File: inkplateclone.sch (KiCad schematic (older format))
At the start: 90 parts, among them J1 ED060SC7, J2 USB_C_Receptacle_USB2.0, J3 Conn_01x03_Male, Q1 Q_NMOS_GSD, Q2 Q_NMOS_GSD, Q3 Q_PMOS_GSD, U1 TPS65186, U2 ED097OC1, U3 MCP23017_SO, U4 ESP32-WROVER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

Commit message: removed polyfuses, fixes #2
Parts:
- removed F1, F2: Polyfuse, Fuse:Fuse_1206_3216Metric, symbol Device:Polyfuse
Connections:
- net +5V: now also J2.A4 (VBUS), J2.A9 (VBUS), J2.B4 (VBUS), J2.B9 (VBUS)
- net VBAT: now also C39.2, U9.5 (BAT)
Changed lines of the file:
@@
 Wire Wire Line
 	2000 9050 2200 9050
-Wire Wire Line
-	2200 9050 2200 8900
 $Comp
 L power:GND #PWR049
@@
 	1    0    0    -1
 $EndComp
-$Comp
-L Device:Polyfuse F1
-U 1 1 5F1AD48B
-P 15500 8600
-F 0 "F1" H 15588 8646 50  0000 L CNN
-F 1 "Polyfuse" H 15588 8555 50  0000 L CNN
-F 2 "Fuse:Fuse_1206_3216Metric" H 15550 8400 50  0001 L CNN
-F 3 "~" H 15500 8600 50  0001 C CNN
-	1    15500 8600
-	1    0    0    -1
-$EndComp
-Connection ~ 15500 8750
 Connection ~ 10100 8350
 Wire Wire Line
@@
 Text GLabel 15500 8400 1    50   Input ~ 0
 VBAT
-Wire Wire Line
-	15500 8400 15500 8450
 Text GLabel 14700 9050 2    50   Input ~ 0
 BAT_TMP
@@
 Wire Notes Line
 	500  7950 16050 7950
-$Comp
-L Device:Polyfuse F2
-U 1 1 5F977BD5
-P 2200 8750
-F 0 "F2" H 2288 8796 50  0000 L CNN
-F 1 "Polyfuse" H 2288 8705 50  0000 L CNN
-F 2 "Fuse:Fuse_1206_3216Metric" H 2250 8550 50  0001 L CNN
-F 3 "~" H 2200 8750 50  0001 C CNN
-	1    2200 8750
-	1    0    0    -1
-$EndComp
 Text Notes 11450 8250 0    100  ~ 0
 Protection and Charger
+Wire Wire Line
+	15500 8400 15500 8750
+Connection ~ 15500 8750
+Wire Wire Line
+	2200 8600 2200 9050
 $EndSCHEMATC

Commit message: replaced LDO, fixes #1
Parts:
- U6: value AMS1117-3.3 -> AP2114H-3.3TRG1
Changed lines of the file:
@@
 P 8550 10300
 F 0 "U6" H 8550 10542 50  0000 C CNN
-F 1 "AMS1117-3.3" H 8550 10451 50  0000 C CNN
+F 1 "AP2114H-3.3TRG1" H 8550 10451 50  0000 C CNN
 F 2 "Package_TO_SOT_SMD:SOT-223-3_TabPin2" H 8550 10500 50  0001 C CNN
 F 3 "http://www.advanced-monolithic.com/pdf/ds1117.pdf" H 8650 10050 50  0001 C CNN

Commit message: routed the usb c serial connection and went to town with alignment
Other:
- moved on the sheet: C29
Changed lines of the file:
@@
 U 1 1 5EADC962
 P 1500 1500
-F 0 "C1" V 1248 1500 50  0000 C CNN
-F 1 "4u7" V 1339 1500 50  0000 C CNN
+F 0 "C1" V 1350 1400 50  0000 C CNN
+F 1 "4u7" V 1350 1600 50  0000 C CNN
 F 2 "Capacitor_SMD:C_0805_2012Metric" H 1538 1350 50  0001 C CNN
 F 3 "~" H 1500 1500 50  0001 C CNN
@@
 U 1 1 5EADDF92
 P 1500 1850
-F 0 "C2" V 1248 1850 50  0000 C CNN
-F 1 "4u7" V 1339 1850 50  0000 C CNN
+F 0 "C2" V 1350 1750 50  0000 C CNN
+F 1 "4u7" V 1350 1950 50  0000 C CNN
 F 2 "Capacitor_SMD:C_0805_2012Metric" H 1538 1700 50  0001 C CNN
 F 3 "~" H 1500 1850 50  0001 C CNN
@@
 U 1 1 5EAE1BDC
 P 1500 2450
-F 0 "C4" V 1248 2450 50  0000 C CNN
-F 1 "10uF" V 1339 2450 50  0000 C CNN
+F 0 "C4" V 1350 2350 50  0000 C CNN
+F 1 "10uF" V 1350 2550 50  0000 C CNN
 F 2 "Capacitor_SMD:C_1206_3216Metric" H 1538 2300 50  0001 C CNN
 F 3 "~" H 1500 2450 50  0001 C CNN
@@
 U 1 1 5EAE31E3
 P 1500 2150
-F 0 "C3" V 1248 2150 50  0000 C CNN
-F 1 "4u7" V 1339 2150 50  0000 C CNN
+F 0 "C3" V 1350 2050 50  0000 C CNN
+F 1 "4u7" V 1350 2250 50  0000 C CNN
 F 2 "Capacitor_SMD:C_0805_2012Metric" H 1538 2000 50  0001 C CNN
 F 3 "~" H 1500 2150 50  0001 C CNN
@@
 U 1 1 5EAE4665
 P 1500 2850
-F 0 "C5" V 1248 2850 50  0000 C CNN
-F 1 "4u7" V 1339 2850 50  0000 C CNN
+F 0 "C5" V 1350 2750 50  0000 C CNN
+F 1 "4u7" V 1350 2950 50  0000 C CNN
 F 2 "Capacitor_SMD:C_0805_2012Metric" H 1538 2700 50  0001 C CNN
 F 3 "~" H 1500 2850 50  0001 C CNN
@@
 U 1 1 5EAE4C72
 P 1500 3050
-F 0 "C6" V 1248 3050 50  0000 C CNN
-F 1 "4u7" V 1339 3050 50  0000 C CNN
+F 0 "C6" V 1650 2950 50  0000 C CNN
+F 1 "4u7" V 1650 3150 50  0000 C CNN
 F 2 "Capacitor_SMD:C_0805_2012Metric" H 1538 2900 50  0001 C CNN
 F 3 "~" H 1500 3050 50  0001 C CNN
@@
 U 1 1 5EB748D6
 P 9350 3300
-F 0 "D4" H 9350 3516 50  0000 C CNN
-F 1 "DIODE SCHOTTKY 30V 1A TSLP-2" H 9350 3425 50  0000 C CNN
+F 0 "D4" H 9350 3200 50  0000 C CNN
+F 1 "DIODE SCHOTTKY 30V 1A TSLP-2" H 9350 3100 50  0000 C CNN
 F 2 "Diode_SMD:D_SOD-323" H 9350 3300 50  0001 C CNN
 F 3 "~" H 9350 3300 50  0001 C CNN
@@
 	1    0    0    -1
 $EndComp
-Text Label 1400 4250 1    50   ~ 0
-I2C_SDA
-Text Label 1150 4250 1    50   ~ 0
-I2C_SCL
-Wire Wire Line
-	1150 3900 1150 4250
-Wire Wire Line
-	1400 4250 1400 3900
+Wire Wire Line
+	1150 3900 1150 3950
+Wire Wire Line
+	1400 3950 1400 3900
 $Comp
 L power:GND #PWR030
@@
 U 1 1 5EB66570
 P 6850 3350
-F 0 "D2" H 6850 3566 50  0000 C CNN
-F 1 "DIODE SCHOTTKY 30V 1A TSLP-2" H 6850 3475 50  0000 C CNN
+F 0 "D2" H 6850 3200 50  0000 C CNN
+F 1 "DIODE SCHOTTKY 30V 1A TSLP-2" H 6850 3100 50  0000 C CNN
 F 2 "Diode_SMD:D_SOD-323" H 6850 3350 50  0001 C CNN
 F 3 "~" H 6850 3350 50  0001 C CNN
@@
 U 1 1 5ED00DE9
 P 2400 9250
-F 0 "R13" V 2193 9250 50  0000 C CNN
-F 1 "5.1K" V 2284 9250 50  0000 C CNN
+F 0 "R13" V 2300 9150 50  0000 C CNN
+F 1 "5.1K" V 2300 9350 50  0000 C CNN
 F 2 "Resistor_SMD:R_0805_2012Metric" V 2330 9250 50  0001 C CNN
 F 3 "~" H 2400 9250 50  0001 C CNN
@@
 U 1 1 5ED01190
 P 2400 9350
-F 0 "R14" V 2193 9350 50  0000 C CNN
-F 1 "5.1K" V 2284 9350 50  0000 C CNN
+F 0 "R14" V 2500 9250 50  0000 C CNN
+F 1 "5.1K" V 2500 9450 50  0000 C CNN
 F 2 "Resistor_SMD:R_0805_2012Metric" V 2330 9350 50  0001 C CNN
 F 3 "~" H 2400 9350 50  0001 C CNN
@@
 L Device:C C29
 U 1 1 5EE33F15
-P 3200 8950
-F 0 "C29" V 3250 9250 50  0000 R CNN
-F 1 "100nF" V 3150 9400 50  0000 R CNN
-F 2 "Capacitor_SMD:C_0805_2012Metric" H 3238 8800 50  0001 C CNN
-F 3 "~" H 3200 8950 50  0001 C CNN
-	1    3200 8950
+P 3300 8750
+F 0 "C29" H 3600 8700 50  0000 R CNN
+F 1 "100nF" H 3650 8800 50  0000 R CNN
+F 2 "Capacitor_SMD:C_0805_2012Metric" H 3338 8600 50  0001 C CNN
+F 3 "~" H 3300 8750 50  0001 C CNN
+	1    3300 8750
 	-1   0    0    1
 $EndComp
@@
 L power:+5V #PWR050
 U 1 1 5EE3442F
-P 3200 8800
-F 0 "#PWR050" H 3200 8650 50  0001 C CNN
-F 1 "+5V" H 3215 8973 50  0000 C CNN
-F 2 "" H 3200 8800 50  0001 C CNN
-F 3 "" H 3200 8800 50  0001 C CNN
-	1    3200 8800
+P 3300 8600
+F 0 "#PWR050" H 3300 8450 50  0001 C CNN
+F 1 "+5V" H 3315 8773 50  0000 C CNN
+F 2 "" H 3300 8600 50  0001 C CNN
+F 3 "" H 3300 8600 50  0001 C CNN
+	1    3300 8600
 	1    0    0    -1
 $EndComp
@@
 L power:GND #PWR051
 U 1 1 5EE34E4D
-P 3200 9100
-F 0 "#PWR051" H 3200 8850 50  0001 C CNN
-F 1 "GND" H 3205 8927 50  0000 C CNN
-F 2 "" H 3200 9100 50  0001 C CNN
-F 3 "" H 3200 9100 50  0001 C CNN
-	1    3200 9100
+P 3300 8900
+F 0 "#PWR051" H 3300 8650 50  0001 C CNN
+F 1 "GND" H 3305 8727 50  0000 C CNN
+F 2 "" H 3300 8900 50  0001 C CNN
+F 3 "" H 3300 8900 50  0001 C CNN
+	1    3300 8900
 	1    0    0    -1
 $EndComp
@@
 Wire Wire Line
 	2200 8600 2200 9050
+Text GLabel 1400 3950 3    50   Input ~ 0
+I2C_SDA
+Text GLabel 1150 3950 3    50   Input ~ 0
+I2C_SCL
 $EndSCHEMATC

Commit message: routed switches and added 3d models
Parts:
- added J4: Conn_01x03_Male, Connector_PinHeader_2.54mm:PinHeader_1x03_P2.54mm_Vertical, symbol Connector:Conn_01x03_Male
- added SW1, SW2: SW_Push, Button_Switch_SMD:SW_Push_1P1T_NO_6x6mm_H9.5mm, symbol Switch:SW_Push
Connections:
- net EPD_CL: now also SW2.1
- net ESP_RXD: now also J4.1 (Pin_1)
- net ESP_TXD: now also J4.2 (Pin_2)
- net GND: now also J4.3 (Pin_3), SW1.2, SW2.2
- net RST: now also SW1.1
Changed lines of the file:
@@
 Wire Wire Line
 	1200 2850 1350 2850
-Text Label 2200 3150 0    50   ~ 0
-I2C_SCL
-Text Label 2200 3250 0    50   ~ 0
-I2C_SDA
-Wire Wire Line
-	2200 3250 2650 3250
-Wire Wire Line
-	2650 3150 2200 3150
+Wire Wire Line
+	2400 3250 2650 3250
+Wire Wire Line
+	2650 3150 2400 3150
 Text Label 2200 3650 0    50   ~ 0
 PWRUP
@@
 Wire Wire Line
 	15400 3900 15200 3900
-Text Label 14350 1450 3    50   ~ 0
-SPI_SCL
-Text Label 14650 1450 3    50   ~ 0
-SPI_NCS
-Text Label 14900 1450 3    50   ~ 0
-SPI_SDI
 Wire Wire Line
 	14650 950  14650 1050
@@
 Text GLabel 1150 3950 3    50   Input ~ 0
 I2C_SCL
+$Comp
+L Switch:SW_Push SW1
+U 1 1 5EC1C6DF
+P 5250 8550
+F 0 "SW1" H 5250 8835 50  0000 C CNN
+F 1 "SW_Push" H 5250 8744 50  0000 C CNN
+F 2 "Button_Switch_SMD:SW_Push_1P1T_NO_6x6mm_H9.5mm" H 5250 8750 50  0001 C CNN
+F 3 "~" H 5250 8750 50  0001 C CNN
+	1    5250 8550
+	1    0    0    -1
+$EndComp
+Text GLabel 4950 8550 0    50   Input ~ 0
+RST
+$Comp
+L power:GND #PWR077
+U 1 1 5EC1F312
+P 5500 8600
+F 0 "#PWR077" H 5500 8350 50  0001 C CNN
+F 1 "GND" H 5505 8427 50  0000 C CNN
+F 2 "" H 5500 8600 50  0001 C CNN
+F 3 "" H 5500 8600 50  0001 C CNN
+	1    5500 8600
+	1    0    0    -1
+$EndComp
+Wire Wire Line
+	5500 8600 5500 8550
+Wire Wire Line
+	5500 8550 5450 8550
+Wire Wire Line
+	5050 8550 4950 8550
+$Comp
+L Switch:SW_Push SW2
+U 1 1 5EC67A54
+P 5400 10100
+F 0 "SW2" H 5400 10385 50  0000 C CNN
+F 1 "SW_Push" H 5400 10294 50  0000 C CNN
+F 2 "Button_Switch_SMD:SW_Push_1P1T_NO_6x6mm_H9.5mm" H 5400 10300 50  0001 C CNN
+F 3 "~" H 5400 10300 50  0001 C CNN
+	1    5400 10100
+	1    0    0    -1
+$EndComp
+$Comp
+L power:GND #PWR078
+U 1 1 5EC6833E
+P 5700 10200
+F 0 "#PWR078" H 5700 9950 50  0001 C CNN
+F 1 "GND" H 5705 10027 50  0000 C CNN
+F 2 "" H 5700 10200 50  0001 C CNN
+F 3 "" H 5700 10200 50  0001 C CNN
+	1    5700 10200
+	1    0    0    -1
+$EndComp
+Text GLabel 5100 10100 0    50   Input ~ 0
+EPD_CL
+Wire Wire Line
+	5100 10100 5200 10100
+Wire Wire Line
+	5600 10100 5700 10100
+Wire Wire Line
+	5700 10100 5700 10200
+$Comp
+L Connector:Conn_01x03_Male J4
+U 1 1 5ECC050B
+P 3850 8500
+F 0 "J4" H 3958 8781 50  0000 C CNN
+F 1 "Conn_01x03_Male" H 3958 8690 50  0000 C CNN
+F 2 "Connector_PinHeader_2.54mm:PinHeader_1x03_P2.54mm_Vertical" H 3850 8500 50  0001 C CNN
+F 3 "~" H 3850 8500 50  0001 C CNN
+	1    3850 8500
+	1    0    0    -1
+$EndComp
+Text GLabel 4150 8400 2    50   Input ~ 0
+ESP_RXD
+Text GLabel 4150 8500 2    50   Input ~ 0
+ESP_TXD
+$Comp
+L power:GND #PWR076
+U 1 1 5ECC394E
+P 4200 8600
+F 0 "#PWR076" H 4200 8350 50  0001 C CNN
+F 1 "GND" H 4205 8427 50  0000 C CNN
+F 2 "" H 4200 8600 50  0001 C CNN
+F 3 "" H 4200 8600 50  0001 C CNN
+	1    4200 8600
+	1    0    0    -1
+$EndComp
+Wire Wire Line
+	4200 8600 4050 8600
+Wire Wire Line
+	4050 8500 4150 8500
+Wire Wire Line
+	4150 8400 4050 8400
+Text GLabel 14350 1450 3    50   Input ~ 0
+SPI_SCL
+Text GLabel 14650 1450 3    50   Input ~ 0
+SPI_NCS
+Text GLabel 14900 1450 3    50   Input ~ 0
+SPI_SDI
+Text GLabel 2400 3150 0    50   Input ~ 0
+I2C_SCL
+Text GLabel 2400 3250 0    50   Input ~ 0
+I2C_SDA
 $EndSCHEMATC

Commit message: routed charger and ideal diode
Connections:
- net BAT_POS is gone; now on net VBAT: J3.3 (Pin_3), R20.1
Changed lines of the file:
@@
 	9650 8650 10000 8650
 Wire Wire Line
-	9800 8350 9650 8350
+	9800 8350 9750 8350
 Wire Wire Line
 	10000 9500 10000 8650
@@
 Text GLabel 2400 3250 0    50   Input ~ 0
 I2C_SDA
+Text GLabel 9750 8300 1    50   Input ~ 0
+VBAT
+Wire Wire Line
+	9750 8300 9750 8350
+Connection ~ 9750 8350
+Wire Wire Line
+	9750 8350 9650 8350
 $EndSCHEMATC

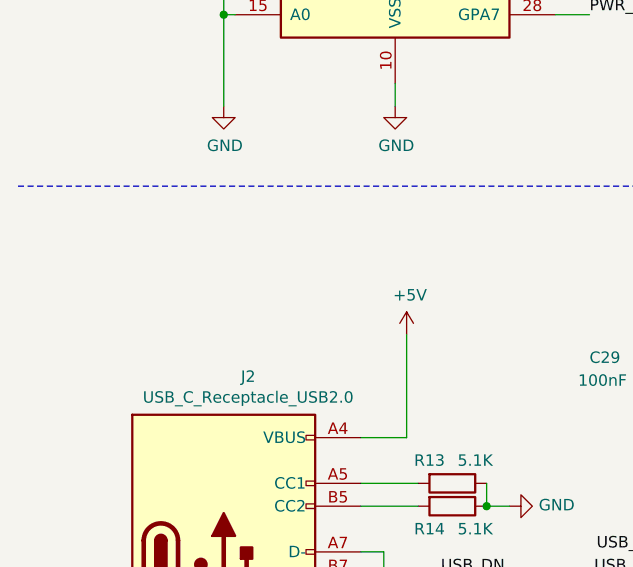
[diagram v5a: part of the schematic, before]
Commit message: routed voltage regulator
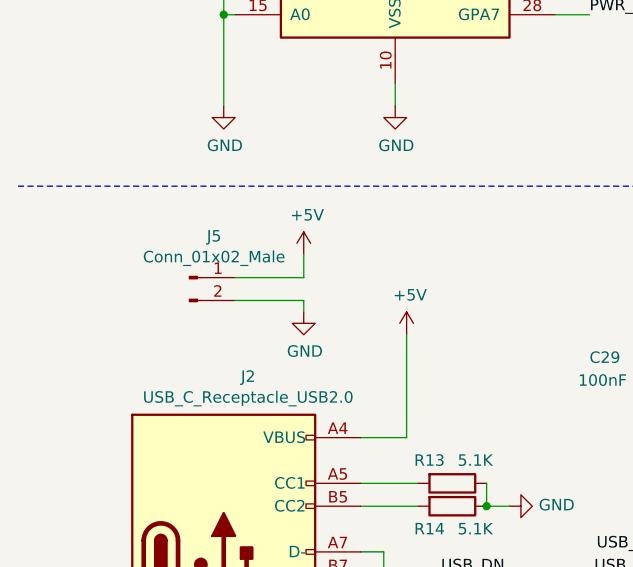
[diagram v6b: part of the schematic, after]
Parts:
- added J5: Conn_01x02_Male, Connector_PinHeader_2.54mm:PinHeader_1x02_P2.54mm_Vertical, symbol Connector:Conn_01x02_Male
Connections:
- net +5V: now also J5.1 (Pin_1)
- net GND: now also J5.2 (Pin_2)
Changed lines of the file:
@@
 Wire Wire Line
 	9750 8350 9650 8350
+$Comp
+L Connector:Conn_01x02_Male J5
+U 1 1 5EE95EB3
+P 1250 8350
+F 0 "J5" H 1358 8531 50  0000 C CNN
+F 1 "Conn_01x02_Male" H 1358 8440 50  0000 C CNN
+F 2 "Connector_PinHeader_2.54mm:PinHeader_1x02_P2.54mm_Vertical" H 1250 8350 50  0001 C CNN
+F 3 "~" H 1250 8350 50  0001 C CNN
+	1    1250 8350
+	1    0    0    -1
+$EndComp
+$Comp
+L power:+5V #PWR079
+U 1 1 5EE9636C
+P 1750 8250
+F 0 "#PWR079" H 1750 8100 50  0001 C CNN
+F 1 "+5V" H 1765 8423 50  0000 C CNN
+F 2 "" H 1750 8250 50  0001 C CNN
+F 3 "" H 1750 8250 50  0001 C CNN
+	1    1750 8250
+	1    0    0    -1
+$EndComp
+$Comp
+L power:GND #PWR080
+U 1 1 5EE967F3
+P 1750 8500
+F 0 "#PWR080" H 1750 8250 50  0001 C CNN
+F 1 "GND" H 1755 8327 50  0000 C CNN
+F 2 "" H 1750 8500 50  0001 C CNN
+F 3 "" H 1750 8500 50  0001 C CNN
+	1    1750 8500
+	1    0    0    -1
+$EndComp
+Wire Wire Line
+	1750 8500 1750 8450
+Wire Wire Line
+	1750 8450 1450 8450
+Wire Wire Line
+	1450 8350 1750 8350
+Wire Wire Line
+	1750 8350 1750 8250
 $EndSCHEMATC
